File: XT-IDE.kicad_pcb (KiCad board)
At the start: 2 copper layers, 114.3 x 106.7 mm, 46 parts, among them J1 CONN_3, J2 CONN_3, J3 CONN_2, J4 CONN_2, J5 INTERRUPT, P6 CONN_1, P7 CONN_1, SW1 I/O ADDR, SW2 ROM OPT, U1 74LS573, U10 74LS688, U11 74LS245, U2 74LS573, U3 74LS245, U4 74LS04, U5 74LS32, U6 74LS04, U7 74LS138, U8 74LS688, U9 28C256

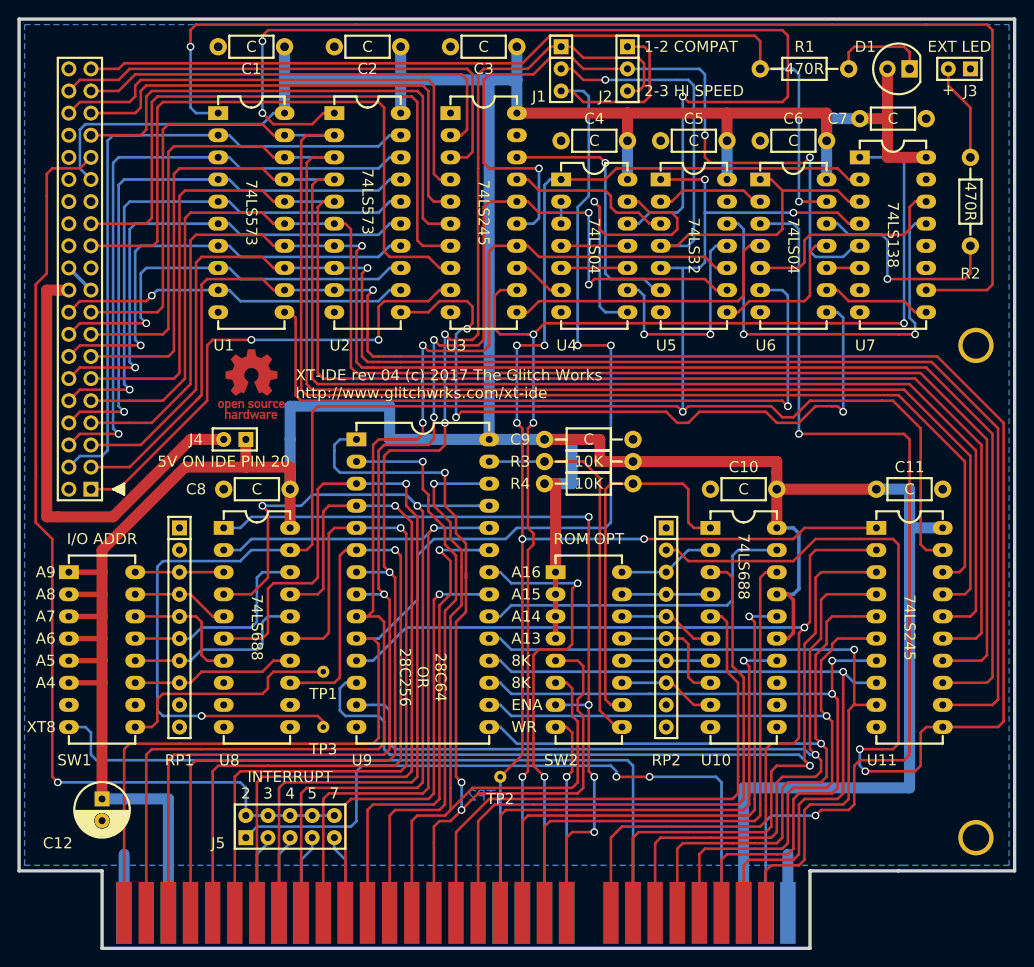
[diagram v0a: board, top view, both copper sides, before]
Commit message: Create Interactive BOM
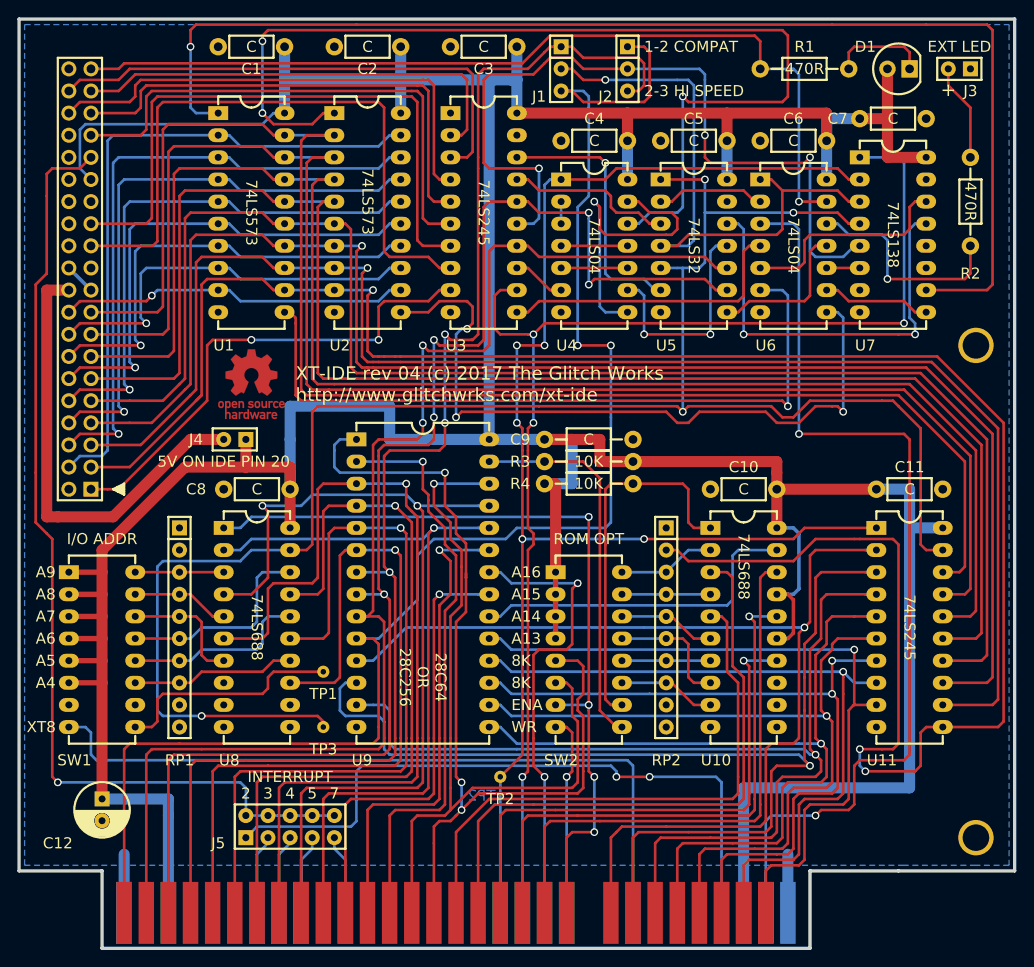
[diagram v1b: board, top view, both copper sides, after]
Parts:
- C12: value 47uF -> 100uF
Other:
- net class Default removed
- net class Power removed
